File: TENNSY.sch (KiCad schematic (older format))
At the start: 48 parts, among them J1 HEADER_2, J2 HEADER_2, J3 Conn_01X03, J4 TB_1X2, Q1 2N7002, Q2 2N7002, Q3 2N7002, SW1 SW_DIP_x02, U1 Teensy4.0, U2 DRV8872, U3 QRE1113, U4 QRE1113, U5 QRE1113, U6 QRE1113, U7 QRE1113, U8 DRV8872, U9 LM1117-SOT

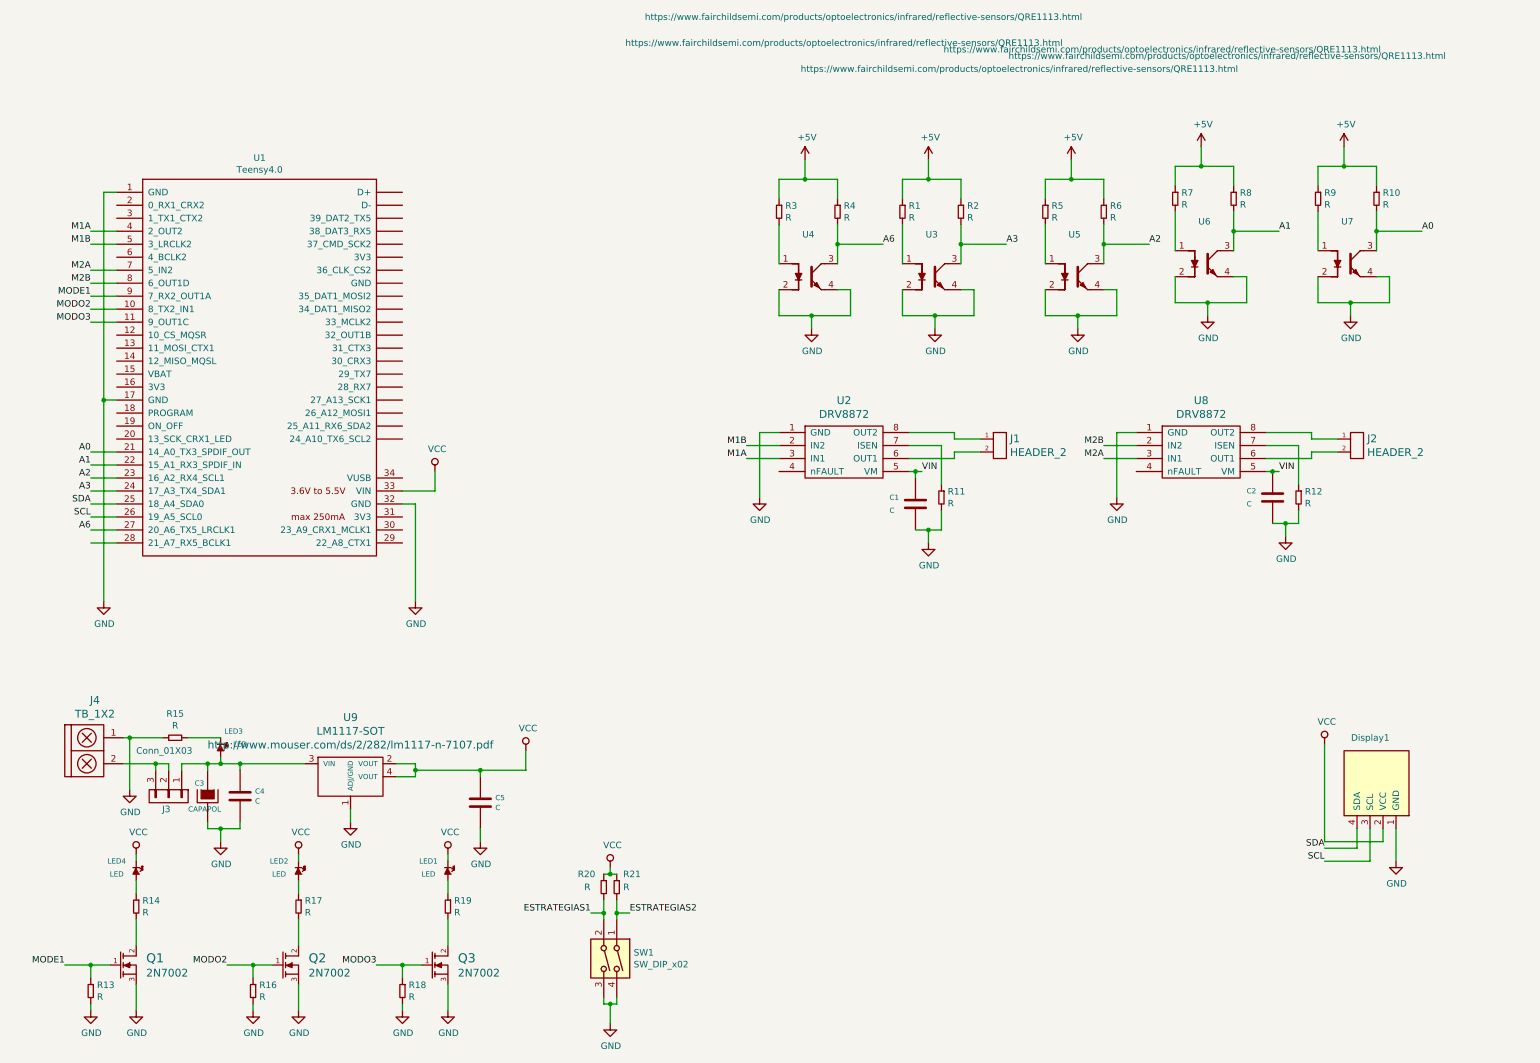
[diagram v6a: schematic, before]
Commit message: modificaciones
se termino pcb,se agregaron: buzzer,imagen de sch de un modulo gitoscopio
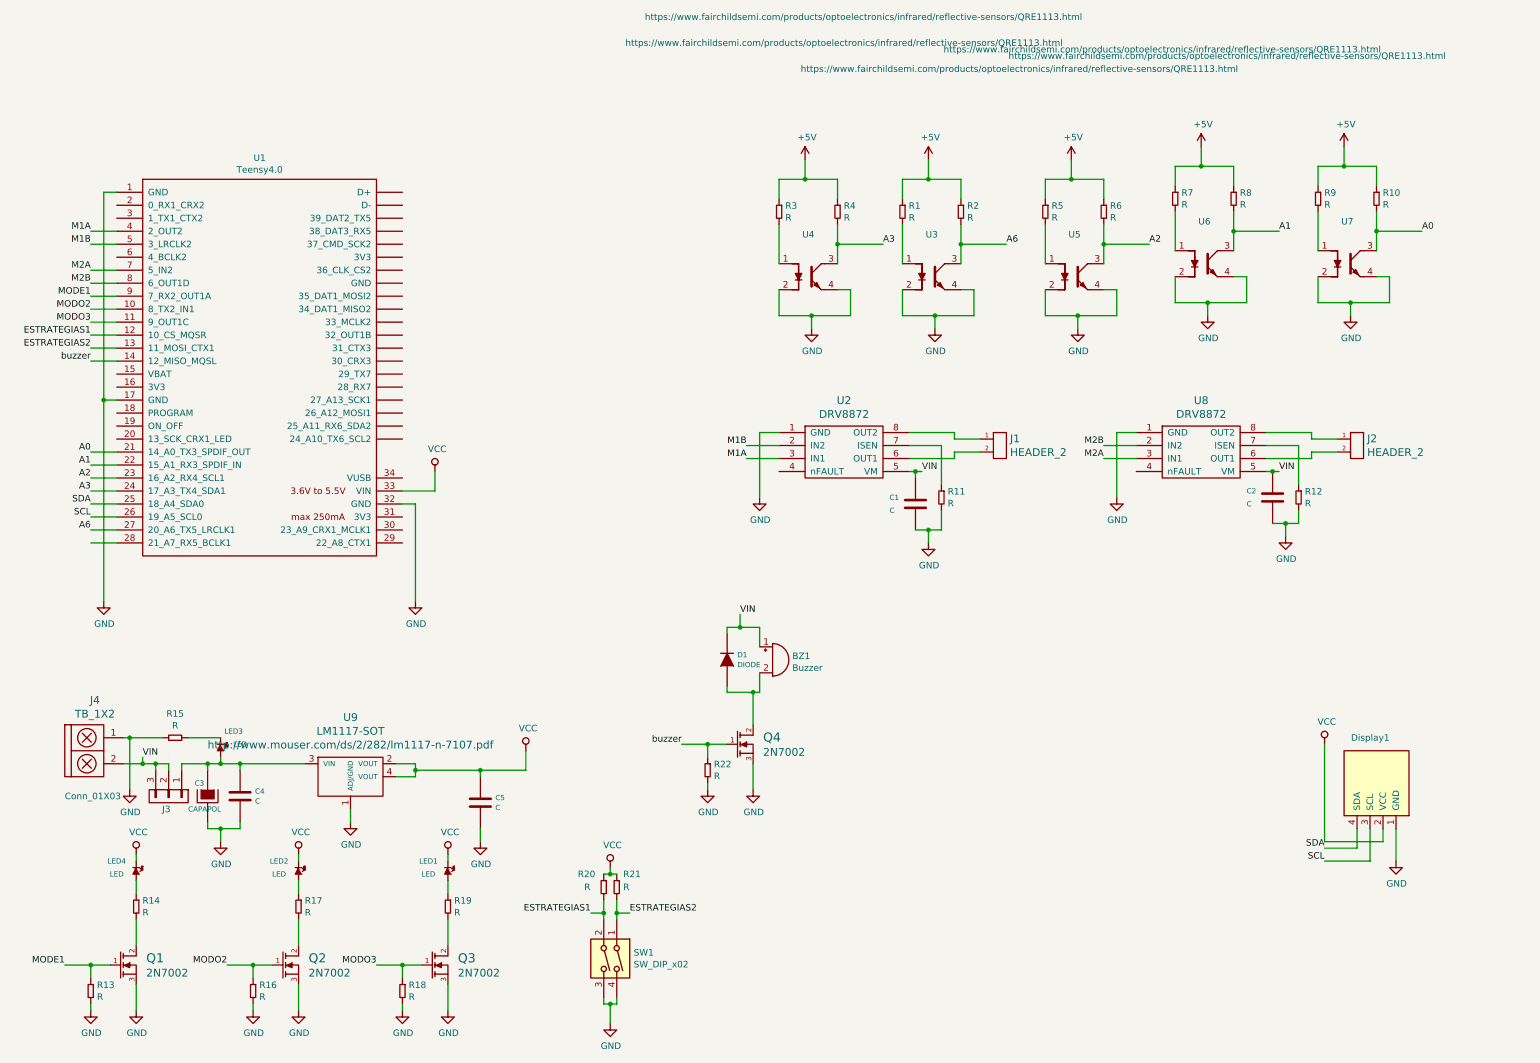
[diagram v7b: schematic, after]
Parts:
- added BZ1: Buzzer, EESTN5:Buzzer_12mm, symbol EESTN5:Buzzer
- added D1: DIODE, EESTN5:sod123, symbol EESTN5:DIODE
- added Q4: 2N7002, EESTN5:SOT23, symbol EESTN5:2N7002
- added R22: R, EESTN5:R_1206, symbol EESTN5:R
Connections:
- net A3: now also R4.2, U4.3; no longer R2.2, U3.3
- net A6: now also R2.2, U3.3; no longer R4.2, U4.3
- net ESTRATEGIAS1: now also U1.12 (10_CS_MQSR)
- net ESTRATEGIAS2: now also U1.13 (11_MOSI_CTX1)
- net GND: now also Q4.3 (S), R22.2
- net VIN: now also J3.2 (P2), J3.3 (P3), J4.2, BZ1.1 (-), D1.2 (K)
- net buzzer: now reaches U1.14 (12_MISO_MQSL)
- net buzzer: now also Q4.1 (G), R22.1
- new net: BZ1.2 (+), D1.1 (A), Q4.2 (D)
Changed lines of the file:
@@
 Text Label 11100 1350 0    50   ~ 0
 A0
-Text Label 6950 1450 0    50   ~ 0
-A6
 Text Label 7900 1450 0    50   ~ 0
+A6
+Text Label 6950 1450 0    50   ~ 0
 A3
 Text Label 9000 1450 0    50   ~ 0
@@
 P 1450 5700
 F 0 "J3" V 1550 5650 50  0000 L CNN
-F 1 "Conn_01X03" V 1100 5450 50  0000 L CNN
+F 1 "Conn_01X03" V 1450 4900 50  0000 L CNN
 F 2 "EESTN5:Pin_Strip_3" H 1450 5700 50  0001 C CNN
 F 3 "" H 1450 5700 50  0001 C CNN
@@
 $EndComp
 Wire Wire Line
-	1100 5450 1350 5450
+	1100 5450 1250 5450
 Wire Wire Line
 	1350 5500 1350 5450
@@
 	1    0    0    -1
 $EndComp
+Wire Wire Line
+	1050 2150 850  2150
+Wire Wire Line
+	850  2250 1050 2250
+Text Label 850  2250 2    50   ~ 0
+ESTRATEGIAS2
+Text Label 850  2150 2    50   ~ 0
+ESTRATEGIAS1
+$Comp
+L EESTN5:R R22
+U 1 1 60F7990D
+P 5600 5500
+F 0 "R22" H 5648 5546 50  0000 L CNN
+F 1 "R" H 5648 5455 50  0000 L CNN
+F 2 "EESTN5:R_1206" H 5600 5500 60  0001 C CNN
+F 3 "" H 5600 5500 60  0000 C CNN
+	1    5600 5500
+	1    0    0    -1
+$EndComp
+$Comp
+L EESTN5:2N7002 Q4
+U 1 1 60F79917
+P 5850 5300
+F 0 "Q4" H 6027 5353 70  0000 L CNN
+F 1 "2N7002" H 6027 5239 60  0000 L CNN
+F 2 "EESTN5:SOT23" H 5850 5300 60  0001 C CNN
+F 3 "" H 5850 5300 60  0000 C CNN
+	1    5850 5300
+	1    0    0    -1
+$EndComp
+Wire Wire Line
+	5950 5450 5950 5650
+$Comp
+L power:GND #PWR0136
+U 1 1 60F79922
+P 5950 5650
+F 0 "#PWR0136" H 5950 5400 50  0001 C CNN
+F 1 "GND" H 5955 5477 50  0000 C CNN
+F 2 "" H 5950 5650 50  0001 C CNN
+F 3 "" H 5950 5650 50  0001 C CNN
+	1    5950 5650
+	1    0    0    -1
+$EndComp
+Wire Wire Line
+	5600 5600 5600 5650
+$Comp
+L power:GND #PWR0137
+U 1 1 60F7992D
+P 5600 5650
+F 0 "#PWR0137" H 5600 5400 50  0001 C CNN
+F 1 "GND" H 5605 5477 50  0000 C CNN
+F 2 "" H 5600 5650 50  0001 C CNN
+F 3 "" H 5600 5650 50  0001 C CNN
+	1    5600 5650
+	1    0    0    -1
+$EndComp
+Wire Wire Line
+	5750 5300 5600 5300
+Wire Wire Line
+	5600 5400 5600 5300
+Connection ~ 5600 5300
+Wire Wire Line
+	5600 5300 5400 5300
+$Comp
+L EESTN5:DIODE D1
+U 1 1 60F8C089
+P 5750 4650
+F 0 "D1" V 5788 4572 40  0000 R CNN
+F 1 "DIODE" V 5712 4572 40  0000 R CNN
+F 2 "EESTN5:sod123" H 5750 4650 60  0001 C CNN
+F 3 "" H 5750 4650 60  0000 C CNN
+	1    5750 4650
+	0    -1   -1   0
+$EndComp
+$Comp
+L EESTN5:Buzzer BZ1
+U 1 1 60F8CADC
+P 6100 4650
+F 0 "BZ1" H 6252 4679 50  0000 L CNN
+F 1 "Buzzer" H 6252 4588 50  0000 L CNN
+F 2 "EESTN5:Buzzer_12mm" V 6075 4750 50  0001 C CNN
+F 3 "" V 6075 4750 50  0001 C CNN
+	1    6100 4650
+	1    0    0    -1
+$EndComp
+Wire Wire Line
+	6000 4550 6000 4400
+Wire Wire Line
+	6000 4400 5850 4400
+Wire Wire Line
+	5750 4450 5750 4400
+Wire Wire Line
+	5750 4850 5750 4900
+Wire Wire Line
+	5750 4900 5950 4900
+Wire Wire Line
+	6000 4900 6000 4750
+Wire Wire Line
+	5950 4900 5950 5150
+Connection ~ 5950 4900
+Wire Wire Line
+	5950 4900 6000 4900
+Wire Wire Line
+	5850 4400 5850 4300
+Connection ~ 5850 4400
+Wire Wire Line
+	5850 4400 5750 4400
+Text Label 1250 5400 0    50   ~ 0
+VIN
+Wire Wire Line
+	1250 5400 1250 5450
+Connection ~ 1250 5450
+Wire Wire Line
+	1250 5450 1350 5450
+Text Label 5850 4300 0    50   ~ 0
+VIN
+Text Label 5400 5300 2    50   ~ 0
+buzzer
+Wire Wire Line
+	850  2350 1050 2350
+Text Label 850  2350 2    50   ~ 0
+buzzer
 $EndSCHEMATC
